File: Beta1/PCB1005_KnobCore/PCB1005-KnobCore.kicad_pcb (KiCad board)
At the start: 2 copper layers, 160 x 46 mm, 44 parts, among them J1 Axoloti_40Pin, U10 OLED_128x32_I2C, U1000 MCP3008T-I/SL, U2 MCP3008T-I/SL, U20 OLED_128x32_I2C, U30 OLED_128x32_I2C, U5 I2C_1x4MUX_TCA9546A

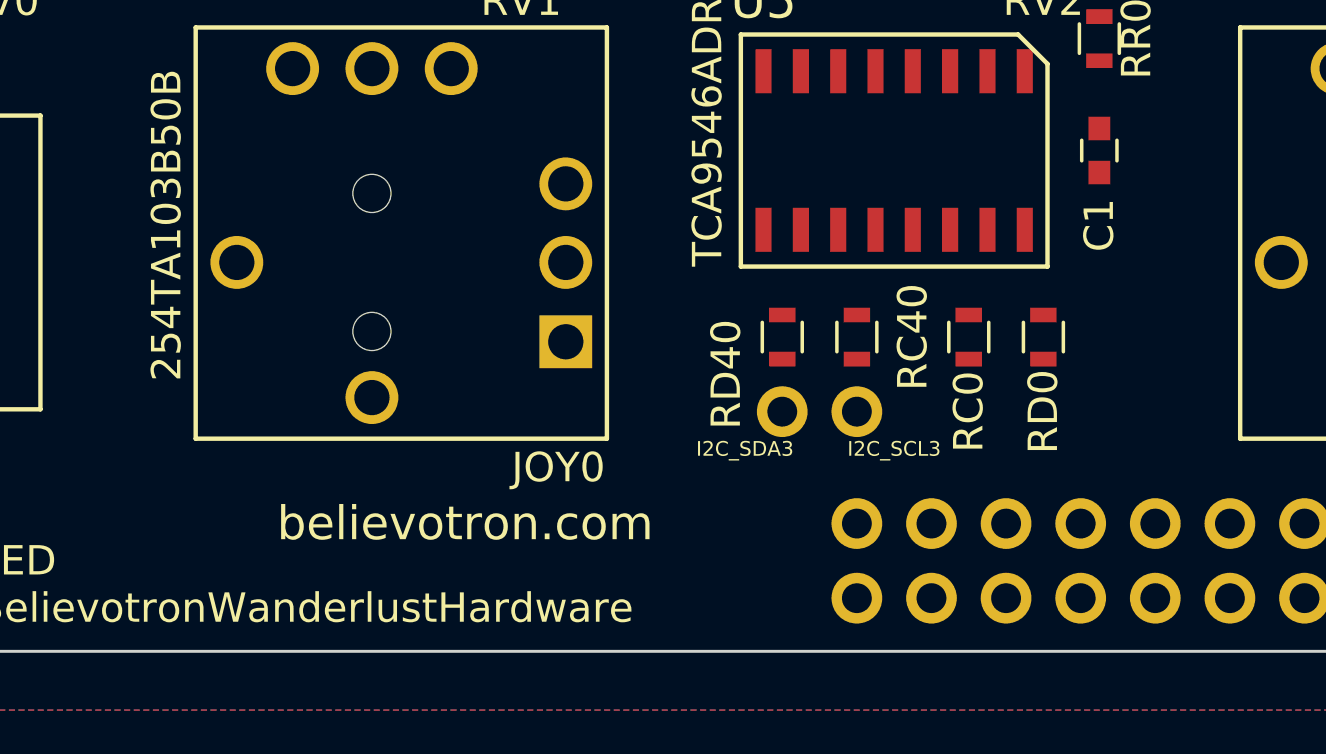
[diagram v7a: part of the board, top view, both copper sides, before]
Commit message: Added extra mounting hole
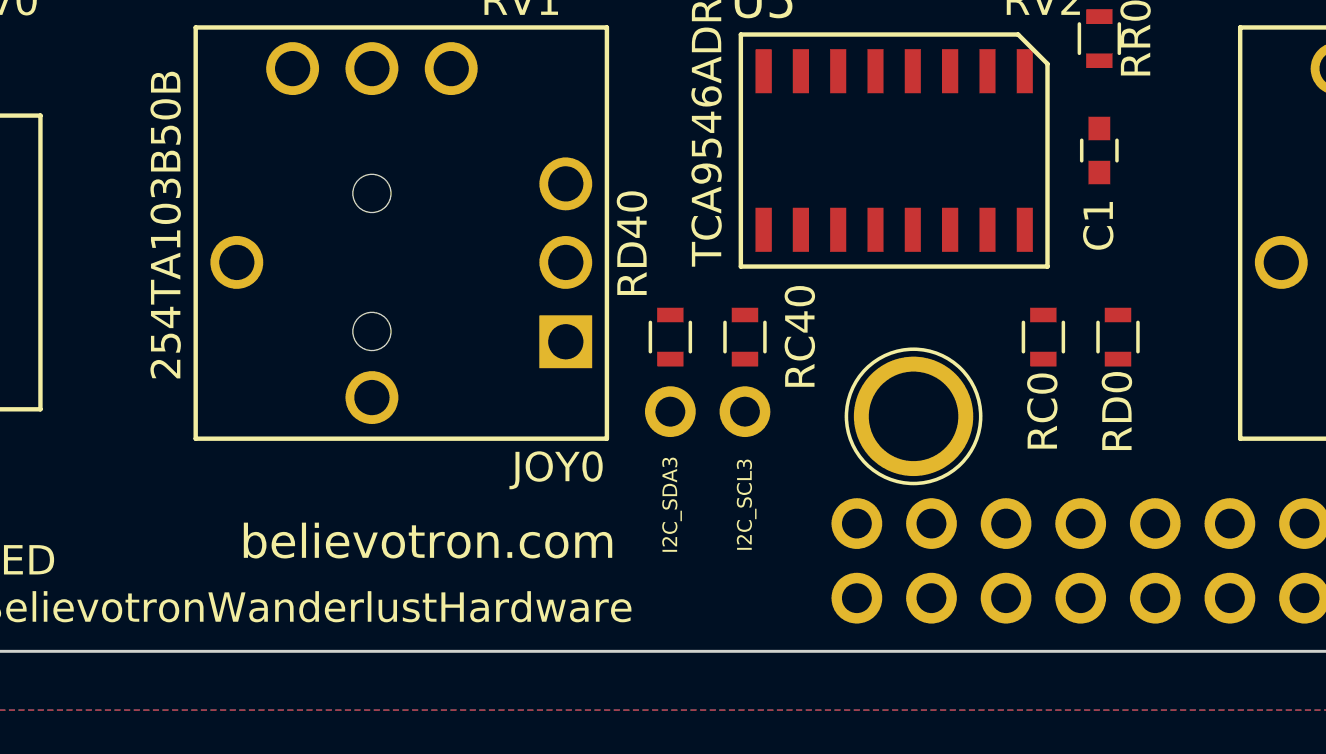
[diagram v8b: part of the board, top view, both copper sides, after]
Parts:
- added REF**: 1pin, Connect:1pin, F.Cu at (54.0, -10.0)
- moved I2C_SCL3 3.81 mm to (48.3, -10.2)
- moved I2C_SDA3 3.81 mm to (45.7, -10.2)
- moved RC40 3.81 mm to (48.3, -12.7)
- moved RD40 3.81 mm to (45.7, -12.7)
- moved RC0 2.54 mm to (58.4, -12.7)
- moved RD0 2.54 mm to (61.0, -12.7)
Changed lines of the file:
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@@
     (tracks 0)
     (zones 0)
-    (modules 44)
+    (modules 45)
     (nets 55)
   )
@@
     (mod_text_size 1 1)
     (mod_text_width 0.15)
-    (pad_size 1.7272 1.7272)
-    (pad_drill 1.016)
+    (pad_size 4.064 4.064)
+    (pad_drill 3.048)
     (pad_to_mask_clearance 0)
     (aux_axis_origin 0 0)
@@
     (add_net "Net-(J1-Pad40)")
   )
+  (module Connect:1pin (layer F.Cu)
+    (at 54 -10)
+    (descr "module 1 pin (ou trou mecanique de percage)")
+    (tags DEV)
+    (fp_text reference REF** (at 0 -3.048) (layer F.SilkS) hide
+      (effects (font (size 1 1) (thickness 0.15)))
+    )
+    (fp_text value 1pin (at 0 3) (layer F.Fab)
+      (effects (font (size 1 1) (thickness 0.15)))
+    )
+    (fp_circle (center 0 0) (end 2 0.8) (layer F.Fab) (width 0.1))
+    (fp_circle (center 0 0) (end 2.6 0) (layer F.CrtYd) (width 0.05))
+    (fp_circle (center 0 0) (end 0 -2.286) (layer F.SilkS) (width 0.12))
+    (pad 1 thru_hole circle (at 0 0) (size 4.064 4.064) (drill 3.048) (layers *.Cu *.Mask))
+  )
   (module Liberry:XY_JOY_254TA103B50B (layer F.Cu)
     (at 71.12 -15.24 180)
@@
   )
   (module Resistors_SMD:R_0603 (layer F.Cu)
-    (at 52.07 -12.7 270)
+    (at 48.26 -12.7 270)
     (descr "Resistor SMD 0603, reflow soldering, Vishay (see dcrcw.pdf)")
     (tags "resistor 0603")
@@
   )
   (module Resistors_SMD:R_0603 (layer F.Cu)
-    (at 49.53 -12.7 270)
+    (at 45.72 -12.7 270)
     (descr "Resistor SMD 0603, reflow soldering, Vishay (see dcrcw.pdf)")
     (tags "resistor 0603")
     (attr smd)
-    (fp_text reference RD40 (at 1.27 1.905 270) (layer F.SilkS)
+    (fp_text reference RD40 (at -3.175 1.27 270) (layer F.SilkS)
       (effects (font (size 1 1) (thickness 0.15)))
     )
@@
   )
   (module Resistors_SMD:R_0603 (layer F.Cu)
-    (at 55.88 -12.7 90)
+    (at 58.42 -12.7 90)
     (descr "Resistor SMD 0603, reflow soldering, Vishay (see dcrcw.pdf)")
     (tags "resistor 0603")
@@
   )
   (module Resistors_SMD:R_0603 (layer F.Cu)
-    (at 58.42 -12.7 90)
+    (at 60.96 -12.7 90)
     (descr "Resistor SMD 0603, reflow soldering, Vishay (see dcrcw.pdf)")
     (tags "resistor 0603")
@@
   )
   (module Liberry:single_0.1 (layer F.Cu)
-    (at 52.07 -10.16 180)
+    (at 48.26 -10.16 180)
     (descr "10 pins through hole IDC header")
     (tags "IDC header socket VASCH")
-    (fp_text reference I2C_SCL3 (at -1.27 -1.27 180) (layer F.SilkS)
+    (fp_text reference I2C_SCL3 (at 0 -3.175 450) (layer F.SilkS)
       (effects (font (size 0.5 0.5) (thickness 0.125)))
     )
@@
   )
   (module Liberry:single_0.1 (layer F.Cu)
-    (at 49.53 -10.16)
+    (at 45.72 -10.16)
     (descr "10 pins through hole IDC header")
     (tags "IDC header socket VASCH")
-    (fp_text reference I2C_SDA3 (at -1.27 1.27) (layer F.SilkS)
+    (fp_text reference I2C_SDA3 (at 0 3.175 90) (layer F.SilkS)
       (effects (font (size 0.5 0.5) (thickness 0.125)))
     )
@@
     (effects (font (size 1 1) (thickness 0.15)))
   )
-  (gr_text believotron.com (at 38.735 -6.35) (layer F.SilkS)
+  (gr_text believotron.com (at 37.465 -5.715) (layer F.SilkS)
     (effects (font (size 1.15 1.15) (thickness 0.15)))
   )
